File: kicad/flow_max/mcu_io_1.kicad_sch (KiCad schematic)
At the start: 1 part, among them U5 MCXN947VDFT

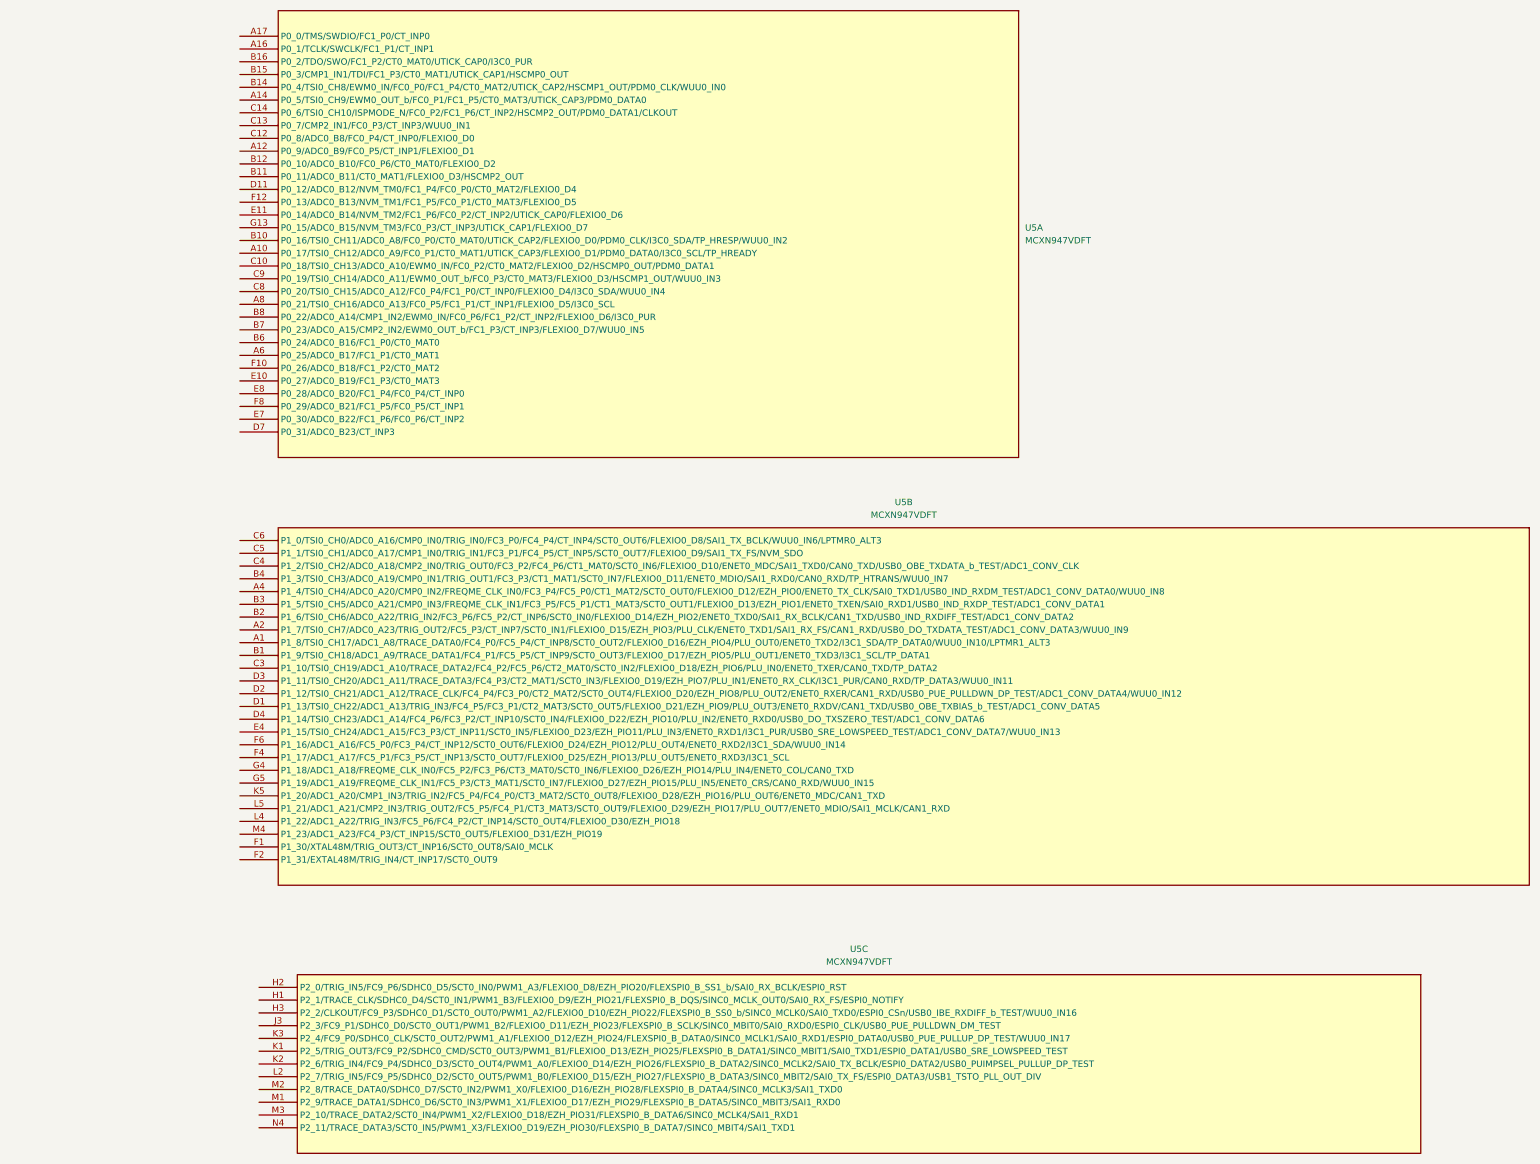
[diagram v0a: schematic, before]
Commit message: Added pin assignment to MCXN947 for the communication lines, Debugger, ISP_Mode and optional GPIO/SD card
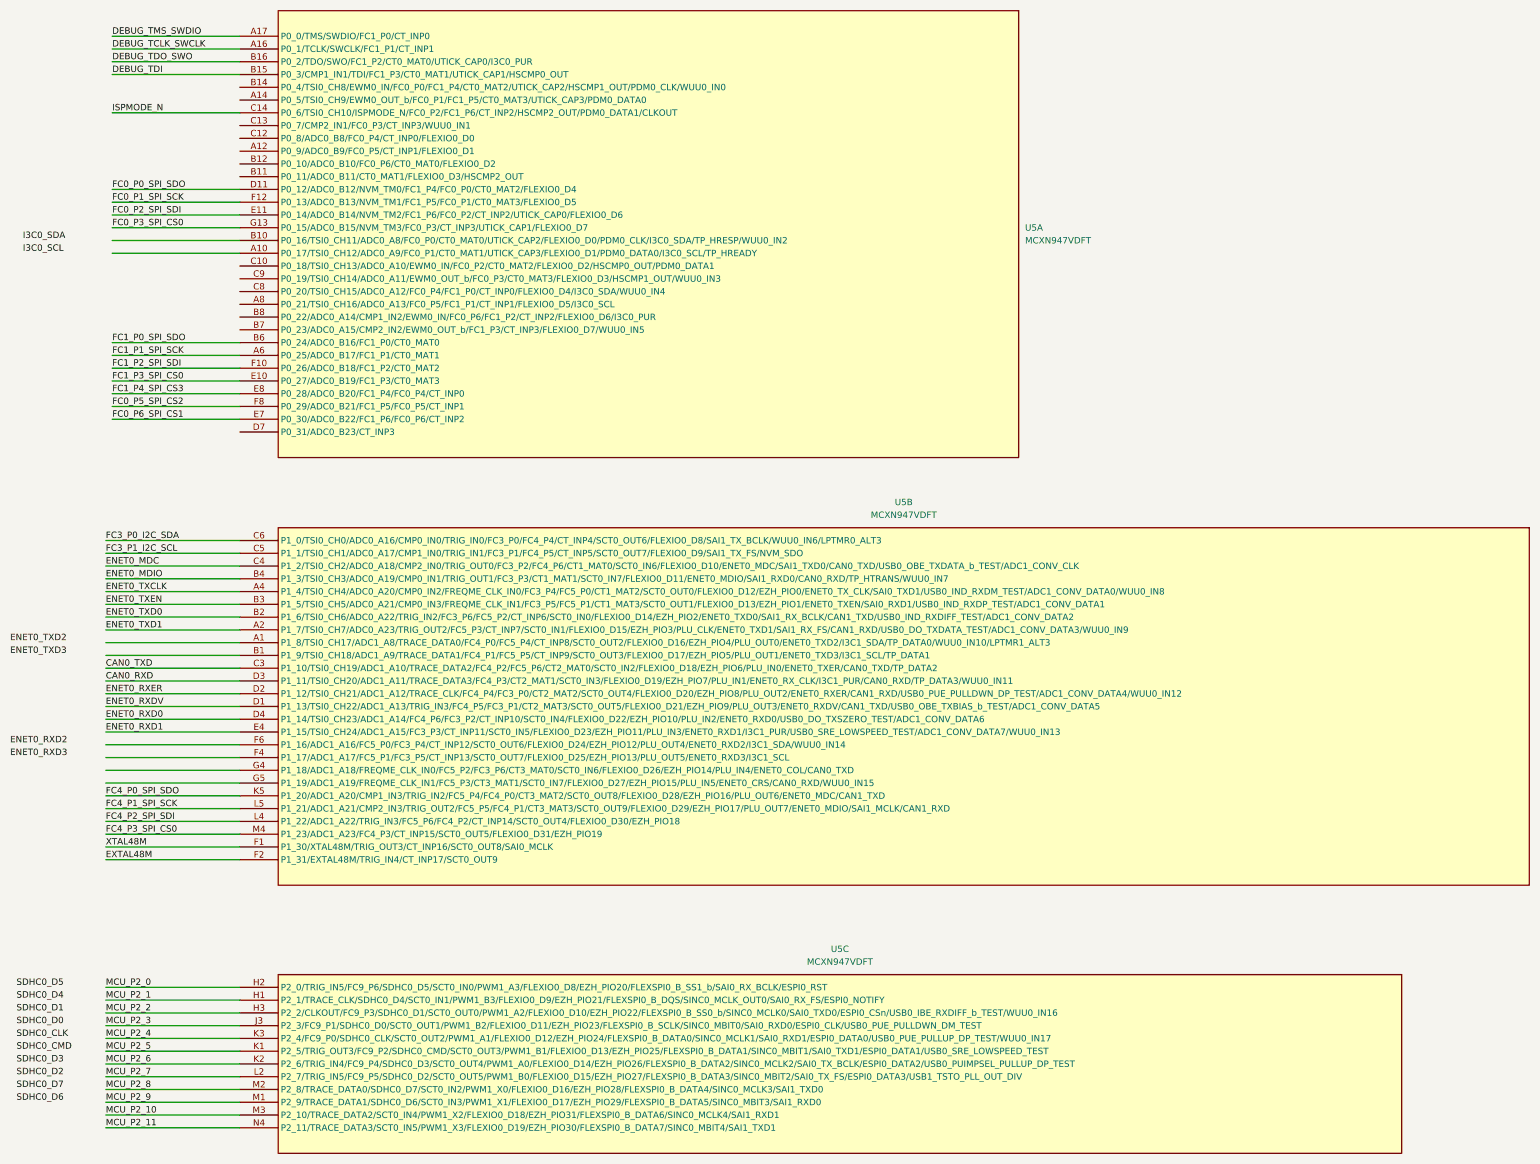
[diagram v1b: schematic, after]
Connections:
- net DEBUG_TCLK_SWCLK: now reaches U5.A16 (P0_1/TCLK/SWCLK/FC1_P1/CT_INP1)
- net DEBUG_TMS_SWDIO: now reaches U5.A17 (P0_0/TMS/SWDIO/FC1_P0/CT_INP0)
- net FC1_P1_SPI_SCK: now reaches U5.A6 (P0_25/ADC0_B17/FC1_P1/CT0_MAT1)
- net DEBUG_TDI: now reaches U5.B15 (P0_3/CMP1_IN1/TDI/FC1_P3/CT0_MAT1/UTICK_CAP1/HSCMP0_OUT)
- net DEBUG_TDO_SWO: now reaches U5.B16 (P0_2/TDO/SWO/FC1_P2/CT0_MAT0/UTICK_CAP0/I3C0_PUR)
- net FC1_P0_SPI_SDO: now reaches U5.B6 (P0_24/ADC0_B16/FC1_P0/CT0_MAT0)
- net ISPMODE_N: now reaches U5.C14 (P0_6/TSI0_CH10/ISPMODE_N/FC0_P2/FC1_P6/CT_INP2/HSCMP2_OUT/PDM0_DATA1/CLKOUT)
- net FC0_P0_SPI_SDO: now reaches U5.D11 (P0_12/ADC0_B12/NVM_TM0/FC1_P4/FC0_P0/CT0_MAT2/FLEXIO0_D4)
- net FC1_P3_SPI_CS0: now reaches U5.E10 (P0_27/ADC0_B19/FC1_P3/CT0_MAT3)
- net FC0_P2_SPI_SDI: now reaches U5.E11 (P0_14/ADC0_B14/NVM_TM2/FC1_P6/FC0_P2/CT_INP2/UTICK_CAP0/FLEXIO0_D6)
- net FC0_P6_SPI_CS1: now reaches U5.E7 (P0_30/ADC0_B22/FC1_P6/FC0_P6/CT_INP2)
- net FC1_P4_SPI_CS3: now reaches U5.E8 (P0_28/ADC0_B20/FC1_P4/FC0_P4/CT_INP0)
- net FC1_P2_SPI_SDI: now reaches U5.F10 (P0_26/ADC0_B18/FC1_P2/CT0_MAT2)
- net FC0_P1_SPI_SCK: now reaches U5.F12 (P0_13/ADC0_B13/NVM_TM1/FC1_P5/FC0_P1/CT0_MAT3/FLEXIO0_D5)
- net FC0_P5_SPI_CS2: now reaches U5.F8 (P0_29/ADC0_B21/FC1_P5/FC0_P5/CT_INP1)
- net FC0_P3_SPI_CS0: now reaches U5.G13 (P0_15/ADC0_B15/NVM_TM3/FC0_P3/CT_INP3/UTICK_CAP1/FLEXIO0_D7)
- net ENET0_TXD1: now reaches U5.A2 (P1_7/TSI0_CH7/ADC0_A23/TRIG_OUT2/FC5_P3/CT_INP7/SCT0_IN1/FLEXIO0_D15/EZH_PIO3/PLU_CLK/ENET0_TXD1/SAI1_RX_FS/CAN1_RXD/USB0_DO_TXDATA_TEST/ADC1_CONV_DATA3/WUU0_IN9)
- net ENET0_TXCLK: now reaches U5.A4 (P1_4/TSI0_CH4/ADC0_A20/CMP0_IN2/FREQME_CLK_IN0/FC3_P4/FC5_P0/CT1_MAT2/SCT0_OUT0/FLEXIO0_D12/EZH_PIO0/ENET0_TX_CLK/SAI0_TXD1/USB0_IND_RXDM_TEST/ADC1_CONV_DATA0/WUU0_IN8)
- net ENET0_TXD0: now reaches U5.B2 (P1_6/TSI0_CH6/ADC0_A22/TRIG_IN2/FC3_P6/FC5_P2/CT_INP6/SCT0_IN0/FLEXIO0_D14/EZH_PIO2/ENET0_TXD0/SAI1_RX_BCLK/CAN1_TXD/USB0_IND_RXDIFF_TEST/ADC1_CONV_DATA2)
- net ENET0_TXEN: now reaches U5.B3 (P1_5/TSI0_CH5/ADC0_A21/CMP0_IN3/FREQME_CLK_IN1/FC3_P5/FC5_P1/CT1_MAT3/SCT0_OUT1/FLEXIO0_D13/EZH_PIO1/ENET0_TXEN/SAI0_RXD1/USB0_IND_RXDP_TEST/ADC1_CONV_DATA1)
- net ENET0_MDIO: now reaches U5.B4 (P1_3/TSI0_CH3/ADC0_A19/CMP0_IN1/TRIG_OUT1/FC3_P3/CT1_MAT1/SCT0_IN7/FLEXIO0_D11/ENET0_MDIO/SAI1_RXD0/CAN0_RXD/TP_HTRANS/WUU0_IN7)
- net CAN0_TXD: now reaches U5.C3 (P1_10/TSI0_CH19/ADC1_A10/TRACE_DATA2/FC4_P2/FC5_P6/CT2_MAT0/SCT0_IN2/FLEXIO0_D18/EZH_PIO6/PLU_IN0/ENET0_TXER/CAN0_TXD/TP_DATA2)
- net ENET0_MDC: now reaches U5.C4 (P1_2/TSI0_CH2/ADC0_A18/CMP2_IN0/TRIG_OUT0/FC3_P2/FC4_P6/CT1_MAT0/SCT0_IN6/FLEXIO0_D10/ENET0_MDC/SAI1_TXD0/CAN0_TXD/USB0_OBE_TXDATA_b_TEST/ADC1_CONV_CLK)
- net FC3_P1_I2C_SCL: now reaches U5.C5 (P1_1/TSI0_CH1/ADC0_A17/CMP1_IN0/TRIG_IN1/FC3_P1/FC4_P5/CT_INP5/SCT0_OUT7/FLEXIO0_D9/SAI1_TX_FS/NVM_SDO)
- net FC3_P0_I2C_SDA: now reaches U5.C6 (P1_0/TSI0_CH0/ADC0_A16/CMP0_IN0/TRIG_IN0/FC3_P0/FC4_P4/CT_INP4/SCT0_OUT6/FLEXIO0_D8/SAI1_TX_BCLK/WUU0_IN6/LPTMR0_ALT3)
- net ENET0_RXDV: now reaches U5.D1 (P1_13/TSI0_CH22/ADC1_A13/TRIG_IN3/FC4_P5/FC3_P1/CT2_MAT3/SCT0_OUT5/FLEXIO0_D21/EZH_PIO9/PLU_OUT3/ENET0_RXDV/CAN1_TXD/USB0_OBE_TXBIAS_b_TEST/ADC1_CONV_DATA5)
- net ENET0_RXER: now reaches U5.D2 (P1_12/TSI0_CH21/ADC1_A12/TRACE_CLK/FC4_P4/FC3_P0/CT2_MAT2/SCT0_OUT4/FLEXIO0_D20/EZH_PIO8/PLU_OUT2/ENET0_RXER/CAN1_RXD/USB0_PUE_PULLDWN_DP_TEST/ADC1_CONV_DATA4/WUU0_IN12)
- net CAN0_RXD: now reaches U5.D3 (P1_11/TSI0_CH20/ADC1_A11/TRACE_DATA3/FC4_P3/CT2_MAT1/SCT0_IN3/FLEXIO0_D19/EZH_PIO7/PLU_IN1/ENET0_RX_CLK/I3C1_PUR/CAN0_RXD/TP_DATA3/WUU0_IN11)
- net ENET0_RXD0: now reaches U5.D4 (P1_14/TSI0_CH23/ADC1_A14/FC4_P6/FC3_P2/CT_INP10/SCT0_IN4/FLEXIO0_D22/EZH_PIO10/PLU_IN2/ENET0_RXD0/USB0_DO_TXSZERO_TEST/ADC1_CONV_DATA6)
- net ENET0_RXD1: now reaches U5.E4 (P1_15/TSI0_CH24/ADC1_A15/FC3_P3/CT_INP11/SCT0_IN5/FLEXIO0_D23/EZH_PIO11/PLU_IN3/ENET0_RXD1/I3C1_PUR/USB0_SRE_LOWSPEED_TEST/ADC1_CONV_DATA7/WUU0_IN13)
- net XTAL48M: now reaches U5.F1 (P1_30/XTAL48M/TRIG_OUT3/CT_INP16/SCT0_OUT8/SAI0_MCLK)
- net EXTAL48M: now reaches U5.F2 (P1_31/EXTAL48M/TRIG_IN4/CT_INP17/SCT0_OUT9)
- net FC4_P0_SPI_SDO: now reaches U5.K5 (P1_20/ADC1_A20/CMP1_IN3/TRIG_IN2/FC5_P4/FC4_P0/CT3_MAT2/SCT0_OUT8/FLEXIO0_D28/EZH_PIO16/PLU_OUT6/ENET0_MDC/CAN1_TXD)
- net FC4_P2_SPI_SDI: now reaches U5.L4 (P1_22/ADC1_A22/TRIG_IN3/FC5_P6/FC4_P2/CT_INP14/SCT0_OUT4/FLEXIO0_D30/EZH_PIO18)
- net FC4_P1_SPI_SCK: now reaches U5.L5 (P1_21/ADC1_A21/CMP2_IN3/TRIG_OUT2/FC5_P5/FC4_P1/CT3_MAT3/SCT0_OUT9/FLEXIO0_D29/EZH_PIO17/PLU_OUT7/ENET0_MDIO/SAI1_MCLK/CAN1_RXD)
- net FC4_P3_SPI_CS0: now reaches U5.M4 (P1_23/ADC1_A23/FC4_P3/CT_INP15/SCT0_OUT5/FLEXIO0_D31/EZH_PIO19)
- net MCU_P2_1: now reaches U5.H1 (P2_1/TRACE_CLK/SDHC0_D4/SCT0_IN1/PWM1_B3/FLEXIO0_D9/EZH_PIO21/FLEXSPI0_B_DQS/SINC0_MCLK_OUT0/SAI0_RX_FS/ESPI0_NOTIFY)
- net MCU_P2_0: now reaches U5.H2 (P2_0/TRIG_IN5/FC9_P6/SDHC0_D5/SCT0_IN0/PWM1_A3/FLEXIO0_D8/EZH_PIO20/FLEXSPI0_B_SS1_b/SAI0_RX_BCLK/ESPI0_RST)
- net MCU_P2_2: now reaches U5.H3 (P2_2/CLKOUT/FC9_P3/SDHC0_D1/SCT0_OUT0/PWM1_A2/FLEXIO0_D10/EZH_PIO22/FLEXSPI0_B_SS0_b/SINC0_MCLK0/SAI0_TXD0/ESPI0_CSn/USB0_IBE_RXDIFF_b_TEST/WUU0_IN16)
- net MCU_P2_3: now reaches U5.J3 (P2_3/FC9_P1/SDHC0_D0/SCT0_OUT1/PWM1_B2/FLEXIO0_D11/EZH_PIO23/FLEXSPI0_B_SCLK/SINC0_MBIT0/SAI0_RXD0/ESPI0_CLK/USB0_PUE_PULLDWN_DM_TEST)
- net MCU_P2_5: now reaches U5.K1 (P2_5/TRIG_OUT3/FC9_P2/SDHC0_CMD/SCT0_OUT3/PWM1_B1/FLEXIO0_D13/EZH_PIO25/FLEXSPI0_B_DATA1/SINC0_MBIT1/SAI0_TXD1/ESPI0_DATA1/USB0_SRE_LOWSPEED_TEST)
- net MCU_P2_6: now reaches U5.K2 (P2_6/TRIG_IN4/FC9_P4/SDHC0_D3/SCT0_OUT4/PWM1_A0/FLEXIO0_D14/EZH_PIO26/FLEXSPI0_B_DATA2/SINC0_MCLK2/SAI0_TX_BCLK/ESPI0_DATA2/USB0_PUIMPSEL_PULLUP_DP_TEST)
- net MCU_P2_4: now reaches U5.K3 (P2_4/FC9_P0/SDHC0_CLK/SCT0_OUT2/PWM1_A1/FLEXIO0_D12/EZH_PIO24/FLEXSPI0_B_DATA0/SINC0_MCLK1/SAI0_RXD1/ESPI0_DATA0/USB0_PUE_PULLUP_DP_TEST/WUU0_IN17)
- net MCU_P2_7: now reaches U5.L2 (P2_7/TRIG_IN5/FC9_P5/SDHC0_D2/SCT0_OUT5/PWM1_B0/FLEXIO0_D15/EZH_PIO27/FLEXSPI0_B_DATA3/SINC0_MBIT2/SAI0_TX_FS/ESPI0_DATA3/USB1_TSTO_PLL_OUT_DIV)
- net MCU_P2_9: now reaches U5.M1 (P2_9/TRACE_DATA1/SDHC0_D6/SCT0_IN3/PWM1_X1/FLEXIO0_D17/EZH_PIO29/FLEXSPI0_B_DATA5/SINC0_MBIT3/SAI1_RXD0)
- net MCU_P2_8: now reaches U5.M2 (P2_8/TRACE_DATA0/SDHC0_D7/SCT0_IN2/PWM1_X0/FLEXIO0_D16/EZH_PIO28/FLEXSPI0_B_DATA4/SINC0_MCLK3/SAI1_TXD0)
- net MCU_P2_10: now reaches U5.M3 (P2_10/TRACE_DATA2/SCT0_IN4/PWM1_X2/FLEXIO0_D18/EZH_PIO31/FLEXSPI0_B_DATA6/SINC0_MCLK4/SAI1_RXD1)
- net MCU_P2_11: now reaches U5.N4 (P2_11/TRACE_DATA3/SCT0_IN5/PWM1_X3/FLEXIO0_D19/EZH_PIO30/FLEXSPI0_B_DATA7/SINC0_MBIT4/SAI1_TXD1)
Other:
- moved on the sheet: U5C

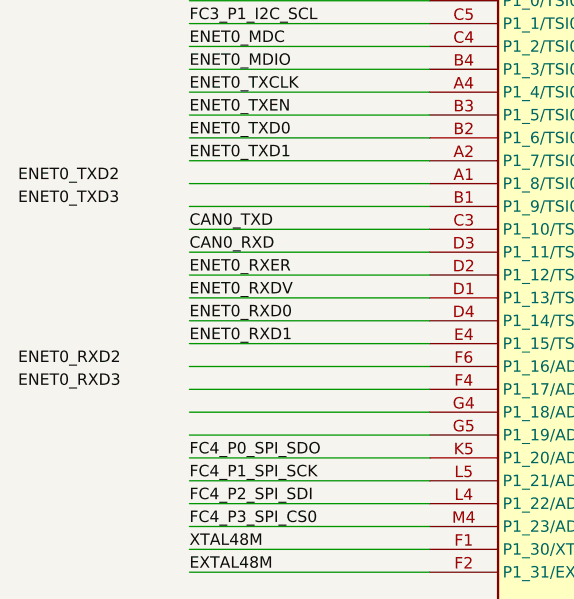
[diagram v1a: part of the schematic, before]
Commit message: Added in the schematic common mode choke filters and TVS diodes to parts where it is needed. Made the polarity protection circuit in schematic. Put placeholders for power supply regulators in schematic.
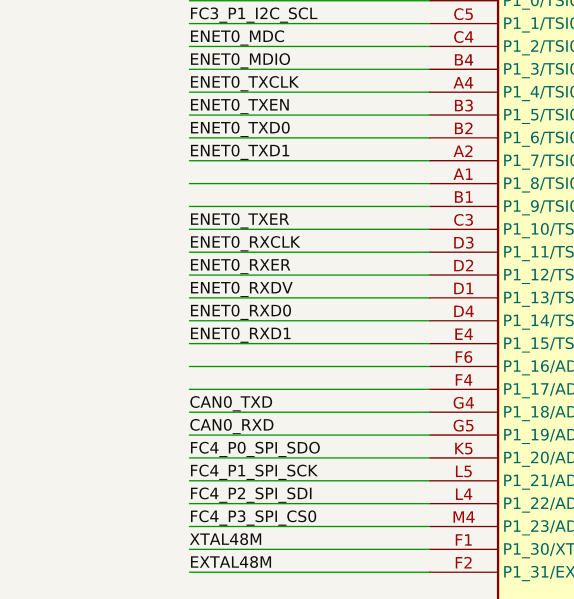
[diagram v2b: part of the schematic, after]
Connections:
- net CAN0_RXD: now also U5.G5 (P1_19/ADC1_A19/FREQME_CLK_IN1/FC5_P3/CT3_MAT1/SCT0_IN7/FLEXIO0_D27/EZH_PIO15/PLU_IN5/ENET0_CRS/CAN0_RXD/WUU0_IN15); no longer U5.D3 (P1_11/TSI0_CH20/ADC1_A11/TRACE_DATA3/FC4_P3/CT2_MAT1/SCT0_IN3/FLEXIO0_D19/EZH_PIO7/PLU_IN1/ENET0_RX_CLK/I3C1_PUR/CAN0_RXD/TP_DATA3/WUU0_IN11)
- net CAN0_TXD: now also U5.G4 (P1_18/ADC1_A18/FREQME_CLK_IN0/FC5_P2/FC3_P6/CT3_MAT0/SCT0_IN6/FLEXIO0_D26/EZH_PIO14/PLU_IN4/ENET0_COL/CAN0_TXD); no longer U5.C3 (P1_10/TSI0_CH19/ADC1_A10/TRACE_DATA2/FC4_P2/FC5_P6/CT2_MAT0/SCT0_IN2/FLEXIO0_D18/EZH_PIO6/PLU_IN0/ENET0_TXER/CAN0_TXD/TP_DATA2)
- new net ENET0_RXCLK: U5.D3 (P1_11/TSI0_CH20/ADC1_A11/TRACE_DATA3/FC4_P3/CT2_MAT1/SCT0_IN3/FLEXIO0_D19/EZH_PIO7/PLU_IN1/ENET0_RX_CLK/I3C1_PUR/CAN0_RXD/TP_DATA3/WUU0_IN11)
- new net ENET0_TXER: U5.C3 (P1_10/TSI0_CH19/ADC1_A10/TRACE_DATA2/FC4_P2/FC5_P6/CT2_MAT0/SCT0_IN2/FLEXIO0_D18/EZH_PIO6/PLU_IN0/ENET0_TXER/CAN0_TXD/TP_DATA2)
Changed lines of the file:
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@@
+		)
+	)
+	(label "ENET0_RXCLK"
+		(at 72.39 152.4 0)
+		(effects
+			(font
+				(size 1.27 1.27)
+			)
+			(justify left bottom)
 		)
 	)
@@
 	)
 	(label "CAN0_TXD"
-		(at 72.39 149.86 0)
-		(effects
-			(font
-				(size 1.27 1.27)
-			)
-			(justify left bottom)
-		)
-	)
-	(label "ENET0_TXD2"
-		(at 53.34 144.78 0)
+		(at 72.39 170.18 0)
 		(effects
 			(font
@@
 		)
 	)
-	(label "ENET0_RXD3"
-		(at 53.34 167.64 0)
-		(effects
-			(font
-				(size 1.27 1.27)
-			)
-			(justify left bottom)
-		)
-	)
 	(label "MCU_P2_1"
 		(at 72.39 215.9 0)
@@
 		)
 	)
+	(label "ENET0_TXER"
+		(at 72.39 149.86 0)
+		(effects
+			(font
+				(size 1.27 1.27)
+			)
+			(justify left bottom)
+		)
+	)
 	(label "FC4_P2_SPI_SDI"
 		(at 72.39 180.34 0)
@@
 	)
 	(label "CAN0_RXD"
-		(at 72.39 152.4 0)
+		(at 72.39 172.72 0)
 		(effects
 			(font
@@
 		(effects
 			(font
-				(size 1.27 1.27)
-			)
-			(justify left bottom)
-		)
-	)
-	(label "ENET0_RXD2"
-		(at 53.34 165.1 0)
-		(effects
-			(font
-				(size 1.27 1.27)
-			)
-			(justify left bottom)
-		)
-	)
-	(label "ENET0_TXD3"
-		(at 53.34 147.32 0)
-		(effects
-			(font
